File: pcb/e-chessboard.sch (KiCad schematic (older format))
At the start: 15 parts

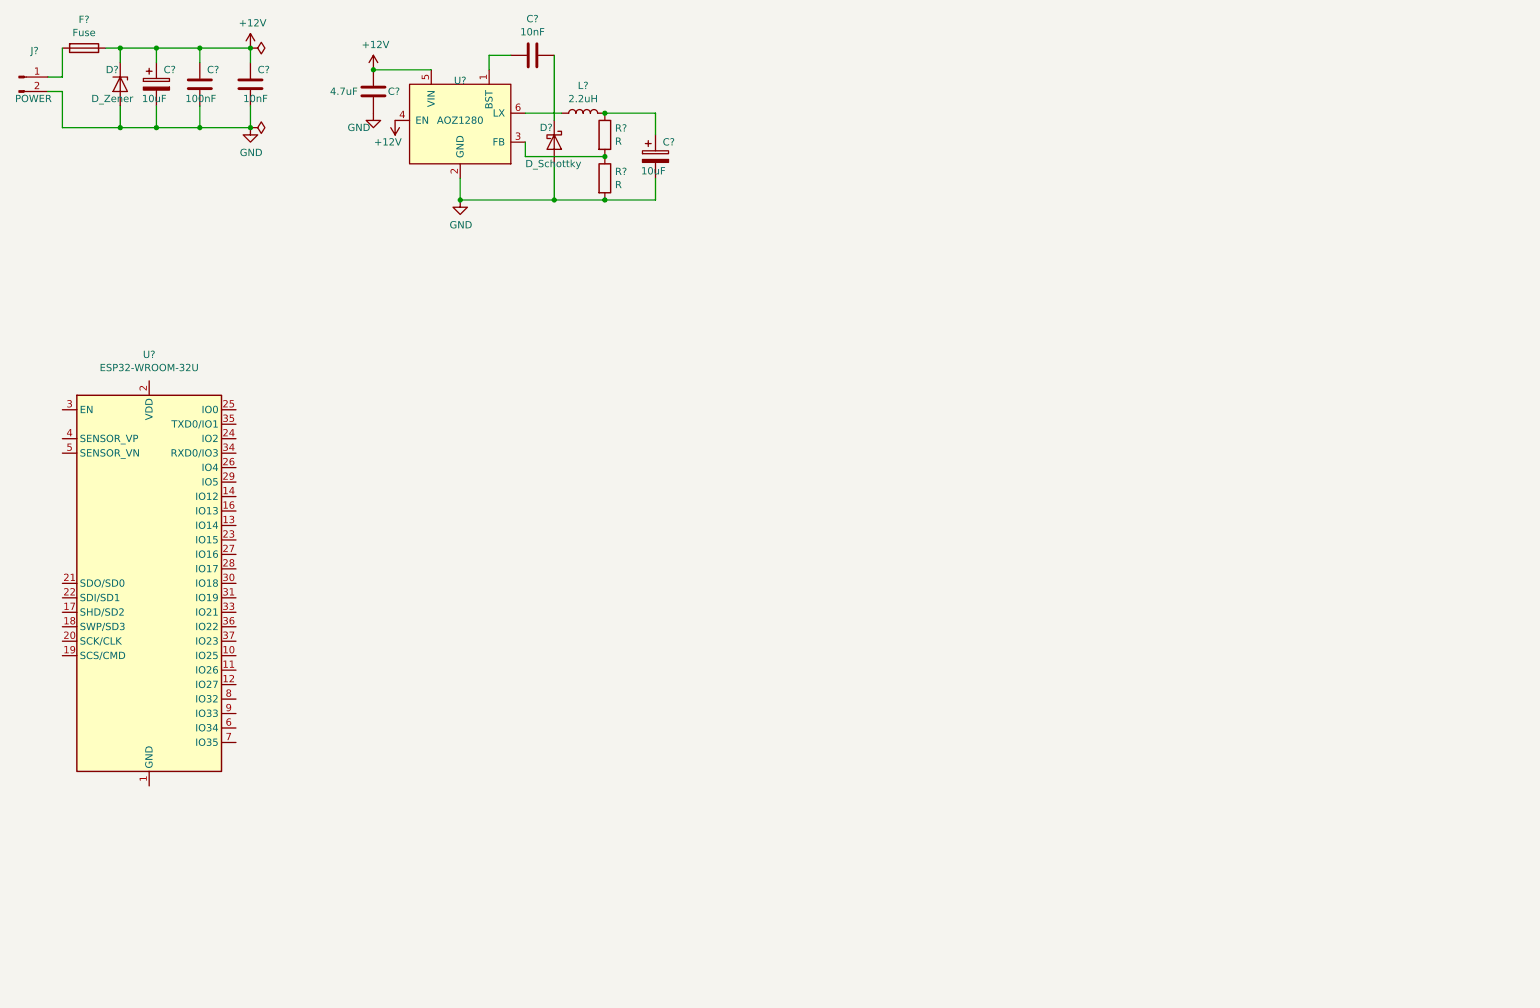
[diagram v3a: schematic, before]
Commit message: feat(kicad): adding magnet matrix and driver
Adding the 3x3 magnet matrix and the NCV7608 driver.
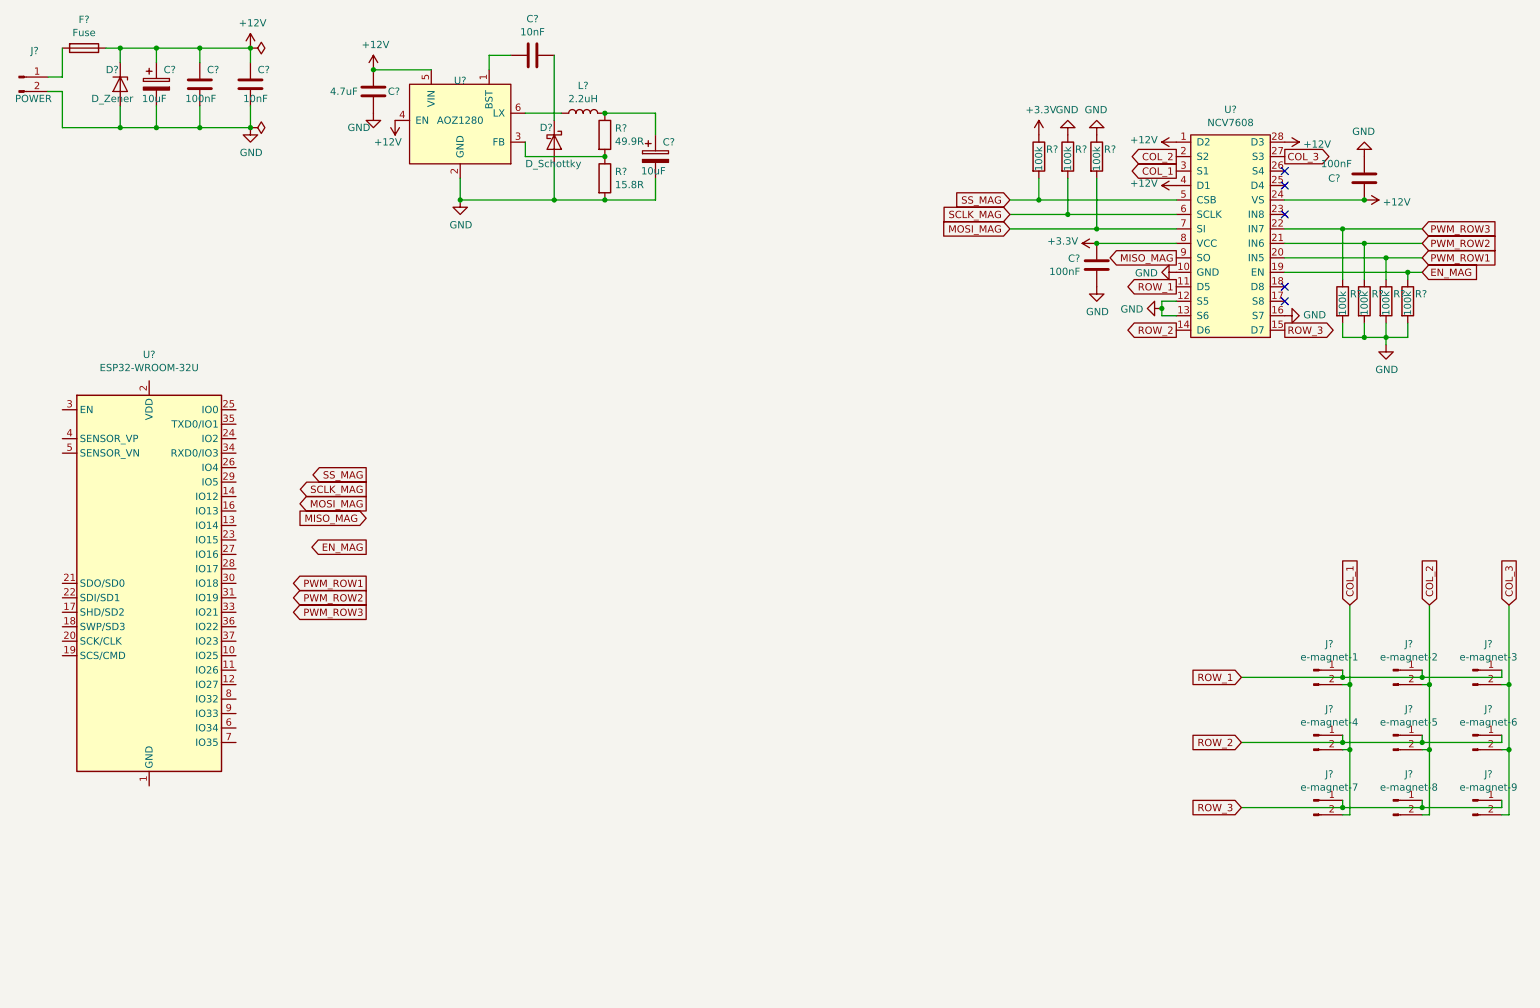
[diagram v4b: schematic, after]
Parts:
- added C? (x2): 100nF, symbol Device:C
- added J?: e-magnet-2, lib_fp:20_15_electromagnet, symbol Connector:Conn_01x02_Male
- added J?: e-magnet-5, lib_fp:20_15_electromagnet, symbol Connector:Conn_01x02_Male
- added J?: e-magnet-8, lib_fp:20_15_electromagnet, symbol Connector:Conn_01x02_Male
- added J?: e-magnet-4, lib_fp:20_15_electromagnet, symbol Connector:Conn_01x02_Male
- added J?: e-magnet-1, lib_fp:20_15_electromagnet, symbol Connector:Conn_01x02_Male
- added J?: e-magnet-3, lib_fp:20_15_electromagnet, symbol Connector:Conn_01x02_Male
- added J?: e-magnet-7, lib_fp:20_15_electromagnet, symbol Connector:Conn_01x02_Male
- added J?: e-magnet-6, lib_fp:20_15_electromagnet, symbol Connector:Conn_01x02_Male
- added J?: e-magnet-9, lib_fp:20_15_electromagnet, symbol Connector:Conn_01x02_Male
- added R? (x7): 100k, symbol Device:R
- added U?: NCV7608, Package_SO:SOIC-28W_7.5x17.9mm_P1.27mm, symbol lib:NCV7608
- R?: value R -> 49.9R
- R?: value R -> 15.8R
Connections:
- net +12V: now also C?.2, U?.1 (D2), U?.24 (VS), U?.28 (D3), U?.4 (D1)
- net GND: now also C?.1, C?.1, R?.1, R?.1, R?.2, R?.2, R?.2, R?.2, U?.10 (GND), U?.12 (S5), U?.13 (S6), U?.16 (S7)
- new net +3V3: C?.2, R?.1, U?.8 (VCC)
- new net COL_1: J?.2 (Pin_2), J?.2 (Pin_2), J?.2 (Pin_2), U?.3 (S1)
- new net COL_2: J?.2 (Pin_2), J?.2 (Pin_2), J?.2 (Pin_2), U?.2 (S2)
- new net COL_3: J?.2 (Pin_2), J?.2 (Pin_2), J?.2 (Pin_2), U?.27 (S3)
- new net EN_MAG: R?.1, U?.19 (EN)
- new net MISO_MAG: U?.9 (SO)
- new net MOSI_MAG: R?.2, U?.7 (SI)
- new net PWM_ROW1: R?.1, U?.20 (IN5)
- new net PWM_ROW2: R?.1, U?.21 (IN6)
- new net PWM_ROW3: R?.1, U?.22 (IN7)
- new net ROW_1: J?.1 (Pin_1), J?.1 (Pin_1), J?.1 (Pin_1), U?.11 (D5)
- new net ROW_2: J?.1 (Pin_1), J?.1 (Pin_1), J?.1 (Pin_1), U?.14 (D6)
- new net ROW_3: J?.1 (Pin_1), J?.1 (Pin_1), J?.1 (Pin_1), U?.15 (D7)
- new net SCLK_MAG: R?.2, U?.6 (SCLK)
- new net SS_MAG: R?.2, U?.5 (CSB)
- no-connect marks 0 -> 5

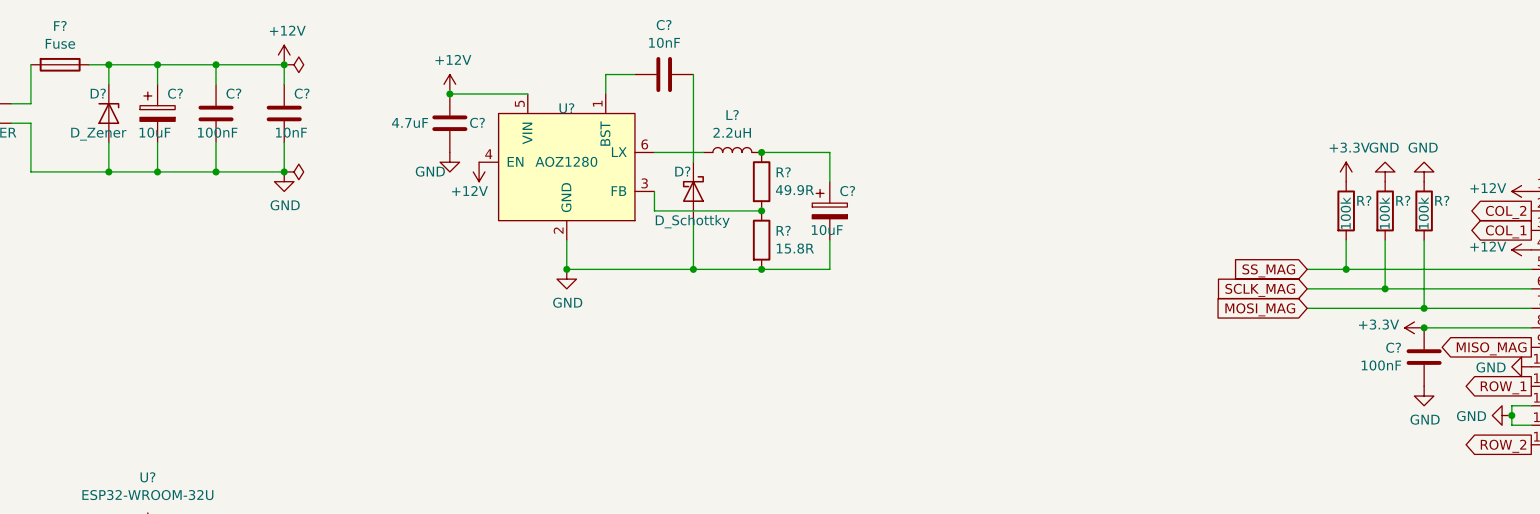
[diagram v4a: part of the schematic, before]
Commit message: fix(kicad): adding missing footprints
Adding C, R, L, D footprints
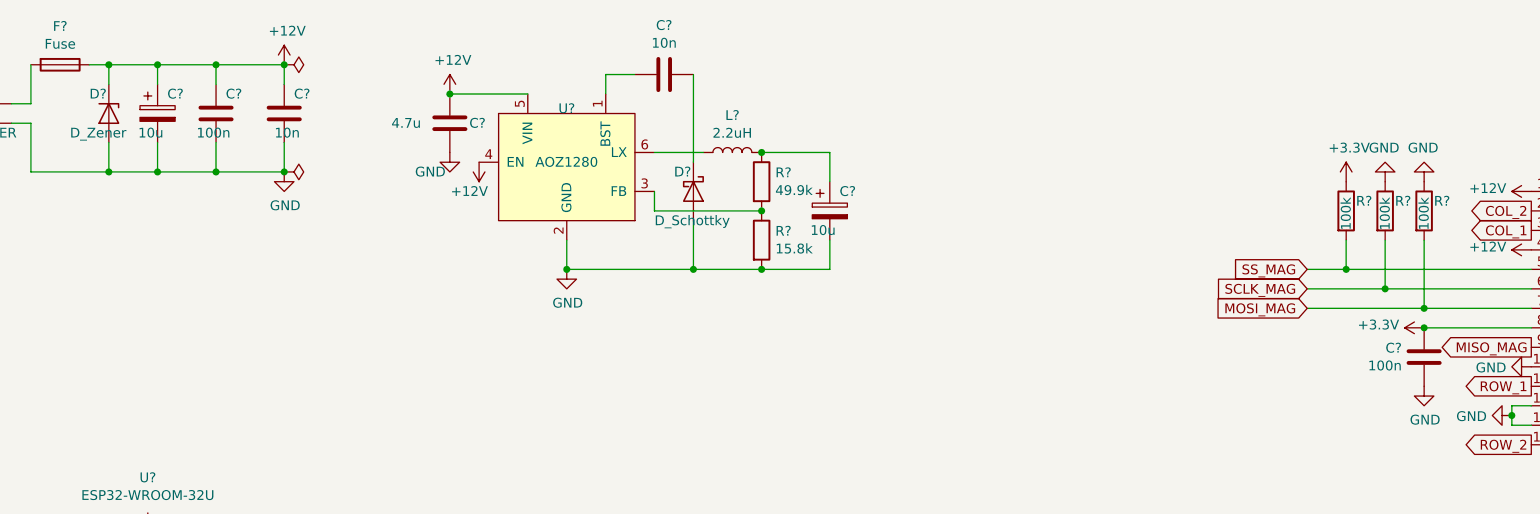
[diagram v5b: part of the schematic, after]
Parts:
- removed R? (x6): 100k, symbol Device:R
- added R? (x6): 100k, Resistor_SMD:R_0805_2012Metric, symbol Device:R
- C? (x2): value 100nF -> 100n; footprint (none) -> Capacitor_SMD:C_0805_2012Metric_Pad1.15x1.40mm_HandSolder
- C? (x2): value 10uF -> 10u; footprint (none) -> Capacitor_Tantalum_SMD:CP_EIA-3528-21_Kemet-B
- C? (x2): value 10nF -> 10n; footprint (none) -> Capacitor_SMD:C_0805_2012Metric_Pad1.15x1.40mm_HandSolder
- C?: value 4.7uF -> 4.7u; footprint (none) -> Capacitor_SMD:C_0805_2012Metric_Pad1.15x1.40mm_HandSolder
- C?: footprint (none) -> Capacitor_SMD:C_0805_2012Metric_Pad1.15x1.40mm_HandSolder
- D?: footprint (none) -> Diode_SMD:D_SOD-123
- D?: footprint (none) -> Diode_SMD:D_SMA
- L?: footprint (none) -> Inductor_SMD:L_Bourns-SRN4018
- R?: value 49.9R -> 49.9k; footprint (none) -> Resistor_SMD:R_0805_2012Metric
- R?: value 15.8R -> 15.8k; footprint (none) -> Resistor_SMD:R_0805_2012Metric
- R?: footprint (none) -> Resistor_SMD:R_0805_2012Metric
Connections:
- net +3V3: now also R?.1
- net EN_MAG: now also R?.1
- net GND: now also R?.1, R?.2, R?.2, R?.2, R?.2
- net PWM_ROW1: now also R?.1
- net PWM_ROW2: now also R?.1
- net PWM_ROW3: now also R?.1
- net SCLK_MAG: now also R?.2
- net SS_MAG: now also R?.2
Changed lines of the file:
@@
 P 1750 1150
 F 0 "C?" H 1800 1250 50  0000 L CNN
-F 1 "100nF" H 1650 1050 50  0000 L CNN
-F 2 "" H 1788 1000 50  0001 C CNN
+F 1 "100n" H 1650 1050 50  0000 L CNN
+F 2 "Capacitor_SMD:C_0805_2012Metric_Pad1.15x1.40mm_HandSolder" H 1788 1000 50  0001 C CNN
 F 3 "~" H 1750 1150 50  0001 C CNN
 	1    1750 1150
@@
 P 1450 1150
 F 0 "C?" H 1500 1250 50  0000 L CNN
-F 1 "10uF" H 1350 1050 50  0000 L CNN
-F 2 "" H 1488 1000 50  0001 C CNN
+F 1 "10u" H 1350 1050 50  0000 L CNN
+F 2 "Capacitor_Tantalum_SMD:CP_EIA-3528-21_Kemet-B" H 1488 1000 50  0001 C CNN
 F 3 "~" H 1450 1150 50  0001 C CNN
 	1    1450 1150
@@
 P 2100 1150
 F 0 "C?" H 2150 1250 50  0000 L CNN
-F 1 "10nF" H 2050 1050 50  0000 L CNN
-F 2 "" H 2138 1000 50  0001 C CNN
+F 1 "10n" H 2050 1050 50  0000 L CNN
+F 2 "Capacitor_SMD:C_0805_2012Metric_Pad1.15x1.40mm_HandSolder" H 2138 1000 50  0001 C CNN
 F 3 "~" H 2100 1150 50  0001 C CNN
 	1    2100 1150
@@
 P 2950 1200
 F 0 "C?" H 3050 1200 50  0000 L CNN
-F 1 "4.7uF" H 2650 1200 50  0000 L CNN
-F 2 "" H 2988 1050 50  0001 C CNN
+F 1 "4.7u" H 2650 1200 50  0000 L CNN
+F 2 "Capacitor_SMD:C_0805_2012Metric_Pad1.15x1.40mm_HandSolder" H 2988 1050 50  0001 C CNN
 F 3 "~" H 2950 1200 50  0001 C CNN
 	1    2950 1200
@@
 P 4050 950
 F 0 "C?" V 4302 950 50  0000 C CNN
-F 1 "10nF" V 4211 950 50  0000 C CNN
-F 2 "" H 4088 800 50  0001 C CNN
+F 1 "10n" V 4211 950 50  0000 C CNN
+F 2 "Capacitor_SMD:C_0805_2012Metric_Pad1.15x1.40mm_HandSolder" H 4088 800 50  0001 C CNN
 F 3 "~" H 4050 950 50  0001 C CNN
 	1    4050 950
@@
 F 0 "L?" V 4590 1350 50  0000 C CNN
 F 1 "2.2uH" V 4499 1350 50  0000 C CNN
-F 2 "" H 4400 1350 50  0001 C CNN
-F 3 "~" H 4400 1350 50  0001 C CNN
+F 2 "Inductor_SMD:L_Bourns-SRN4018" H 4400 1350 50  0001 C CNN
+F 3 "https://www.bourns.com/docs/Product-Datasheets/SRN4018.pdf" H 4400 1350 50  0001 C CNN
 	1    4400 1350
 	0    -1   -1   0
@@
 P 4900 1650
 F 0 "C?" H 4950 1750 50  0000 L CNN
-F 1 "10uF" H 4800 1550 50  0000 L CNN
-F 2 "" H 4938 1500 50  0001 C CNN
+F 1 "10u" H 4800 1550 50  0000 L CNN
+F 2 "Capacitor_Tantalum_SMD:CP_EIA-3528-21_Kemet-B" H 4938 1500 50  0001 C CNN
 F 3 "~" H 4900 1650 50  0001 C CNN
 	1    4900 1650
@@
 P 4550 1500
 F 0 "R?" H 4620 1546 50  0000 L CNN
-F 1 "49.9R" H 4620 1455 50  0000 L CNN
-F 2 "" V 4480 1500 50  0001 C CNN
+F 1 "49.9k" H 4620 1455 50  0000 L CNN
+F 2 "Resistor_SMD:R_0805_2012Metric" V 4480 1500 50  0001 C CNN
 F 3 "~" H 4550 1500 50  0001 C CNN
 	1    4550 1500
@@
 P 4550 1800
 F 0 "R?" H 4620 1846 50  0000 L CNN
-F 1 "15.8R" H 4620 1755 50  0000 L CNN
-F 2 "" V 4480 1800 50  0001 C CNN
+F 1 "15.8k" H 4620 1755 50  0000 L CNN
+F 2 "Resistor_SMD:R_0805_2012Metric" V 4480 1800 50  0001 C CNN
 F 3 "~" H 4550 1800 50  0001 C CNN
 	1    4550 1800
@@
 F 0 "D?" V 4100 1450 50  0000 L CNN
 F 1 "D_Schottky" V 4350 1350 50  0000 L CNN
-F 2 "" H 4200 1550 50  0001 C CNN
+F 2 "Diode_SMD:D_SOD-123" H 4200 1550 50  0001 C CNN
 F 3 "~" H 4200 1550 50  0001 C CNN
 	1    4200 1550
@@
 F 0 "D?" V 1100 1050 50  0000 L CNN
 F 1 "D_Zener" V 1300 950 50  0000 L CNN
-F 2 "" H 1200 1150 50  0001 C CNN
-F 3 "~" H 1200 1150 50  0001 C CNN
+F 2 "Diode_SMD:D_SMA" H 1200 1150 50  0001 C CNN
+F 3 "https://www.diodes.com/assets/Datasheets/ds18015.pdf" H 1200 1150 50  0001 C CNN
 	1    1200 1150
 	0    1    1    0
@@
 F 0 "C?" H 10050 1800 50  0000 R CNN
 F 1 "100nF" H 10100 1900 50  0000 R CNN
-F 2 "" H 9838 1650 50  0001 C CNN
+F 2 "Capacitor_SMD:C_0805_2012Metric_Pad1.15x1.40mm_HandSolder" H 9838 1650 50  0001 C CNN
 F 3 "~" H 9800 1800 50  0001 C CNN
 	1    9800 1800
@@
 F 0 "R?" H 8000 1700 50  0000 L CNN
 F 1 "100k" V 7950 1550 50  0000 L CNN
-F 2 "" V 7880 1650 50  0001 C CNN
+F 2 "Resistor_SMD:R_0805_2012Metric" V 7880 1650 50  0001 C CNN
 F 3 "~" H 7950 1650 50  0001 C CNN
 	1    7950 1650
-	1    0    0    -1
-$EndComp
-$Comp
-L Device:R R?
-U 1 1 5E6E973A
-P 7750 1650
-F 0 "R?" H 7800 1700 50  0000 L CNN
-F 1 "100k" V 7750 1550 50  0000 L CNN
-F 2 "" V 7680 1650 50  0001 C CNN
-F 3 "~" H 7750 1650 50  0001 C CNN
-	1    7750 1650
-	1    0    0    -1
-$EndComp
-$Comp
-L Device:R R?
-U 1 1 5E6E9902
-P 7550 1650
-F 0 "R?" H 7600 1700 50  0000 L CNN
-F 1 "100k" V 7550 1550 50  0000 L CNN
-F 2 "" V 7480 1650 50  0001 C CNN
-F 3 "~" H 7550 1650 50  0001 C CNN
-	1    7550 1650
 	1    0    0    -1
 $EndComp
@@
 P 7950 2400
 F 0 "C?" H 7836 2354 50  0000 R CNN
-F 1 "100nF" H 7836 2445 50  0000 R CNN
-F 2 "" H 7988 2250 50  0001 C CNN
+F 1 "100n" H 7836 2445 50  0000 R CNN
+F 2 "Capacitor_SMD:C_0805_2012Metric_Pad1.15x1.40mm_HandSolder" H 7988 2250 50  0001 C CNN
 F 3 "~" H 7950 2400 50  0001 C CNN
 	1    7950 2400
@@
 $EndComp
 $Comp
-L Device:R R?
-U 1 1 5E73BE4D
-P 9950 2650
-F 0 "R?" H 10000 2700 50  0000 L CNN
-F 1 "100k" V 9950 2550 50  0000 L CNN
-F 2 "" V 9880 2650 50  0001 C CNN
-F 3 "~" H 9950 2650 50  0001 C CNN
-	1    9950 2650
-	1    0    0    -1
-$EndComp
-$Comp
-L Device:R R?
-U 1 1 5E73C4B3
-P 9800 2650
-F 0 "R?" H 9850 2700 50  0000 L CNN
-F 1 "100k" V 9800 2550 50  0000 L CNN
-F 2 "" V 9730 2650 50  0001 C CNN
-F 3 "~" H 9800 2650 50  0001 C CNN
-	1    9800 2650
-	1    0    0    -1
-$EndComp
-$Comp
-L Device:R R?
-U 1 1 5E73C813
-P 9650 2650
-F 0 "R?" H 9700 2700 50  0000 L CNN
-F 1 "100k" V 9650 2550 50  0000 L CNN
-F 2 "" V 9580 2650 50  0001 C CNN
-F 3 "~" H 9650 2650 50  0001 C CNN
-	1    9650 2650
-	1    0    0    -1
-$EndComp
-$Comp
 L power:GND #PWR?
 U 1 1 5E750D06
@@
 Wire Wire Line
 	9950 2350 9250 2350
+Wire Wire Line
+	9250 1950 9800 1950
+Connection ~ 9800 1950
+Wire Wire Line
+	9950 2350 10200 2350
+Wire Wire Line
+	9800 2250 10200 2250
+Wire Wire Line
+	9650 2150 10200 2150
+Wire Wire Line
+	10200 2450 10100 2450
+Wire Wire Line
+	10100 2500 10100 2450
+Connection ~ 10100 2450
+Wire Wire Line
+	10100 2450 9250 2450
+Wire Wire Line
+	10100 2800 10100 2900
+Wire Wire Line
+	10100 2900 9950 2900
 $Comp
 L Device:R R?
-U 1 1 5E77C75A
+U 1 1 5E850D8B
+P 7750 1650
+F 0 "R?" H 7800 1700 50  0000 L CNN
+F 1 "100k" V 7750 1550 50  0000 L CNN
+F 2 "Resistor_SMD:R_0805_2012Metric" V 7680 1650 50  0001 C CNN
+F 3 "~" H 7750 1650 50  0001 C CNN
+	1    7750 1650
+	1    0    0    -1
+$EndComp
+$Comp
+L Device:R R?
+U 1 1 5E850F87
+P 7550 1650
+F 0 "R?" H 7600 1700 50  0000 L CNN
+F 1 "100k" V 7550 1550 50  0000 L CNN
+F 2 "Resistor_SMD:R_0805_2012Metric" V 7480 1650 50  0001 C CNN
+F 3 "~" H 7550 1650 50  0001 C CNN
+	1    7550 1650
+	1    0    0    -1
+$EndComp
+$Comp
+L Device:R R?
+U 1 1 5E8512EB
+P 9650 2650
+F 0 "R?" H 9700 2700 50  0000 L CNN
+F 1 "100k" V 9650 2550 50  0000 L CNN
+F 2 "Resistor_SMD:R_0805_2012Metric" V 9580 2650 50  0001 C CNN
+F 3 "~" H 9650 2650 50  0001 C CNN
+	1    9650 2650
+	1    0    0    -1
+$EndComp
+$Comp
+L Device:R R?
+U 1 1 5E858158
+P 9800 2650
+F 0 "R?" H 9850 2700 50  0000 L CNN
+F 1 "100k" V 9800 2550 50  0000 L CNN
+F 2 "Resistor_SMD:R_0805_2012Metric" V 9730 2650 50  0001 C CNN
+F 3 "~" H 9800 2650 50  0001 C CNN
+	1    9800 2650
+	1    0    0    -1
+$EndComp
+$Comp
+L Device:R R?
+U 1 1 5E85848F
+P 9950 2650
+F 0 "R?" H 10000 2700 50  0000 L CNN
+F 1 "100k" V 9950 2550 50  0000 L CNN
+F 2 "Resistor_SMD:R_0805_2012Metric" V 9880 2650 50  0001 C CNN
+F 3 "~" H 9950 2650 50  0001 C CNN
+	1    9950 2650
+	1    0    0    -1
+$EndComp
+$Comp
+L Device:R R?
+U 1 1 5E85871C
 P 10100 2650
 F 0 "R?" H 10150 2700 50  0000 L CNN
 F 1 "100k" V 10100 2550 50  0000 L CNN
-F 2 "" V 10030 2650 50  0001 C CNN
+F 2 "Resistor_SMD:R_0805_2012Metric" V 10030 2650 50  0001 C CNN
 F 3 "~" H 10100 2650 50  0001 C CNN
 	1    10100 2650
 	1    0    0    -1
 $EndComp
-Wire Wire Line
-	9250 1950 9800 1950
-Connection ~ 9800 1950
-Wire Wire Line
-	9950 2350 10200 2350
-Wire Wire Line
-	9800 2250 10200 2250
-Wire Wire Line
-	9650 2150 10200 2150
-Wire Wire Line
-	10200 2450 10100 2450
-Wire Wire Line
-	10100 2500 10100 2450
-Connection ~ 10100 2450
-Wire Wire Line
-	10100 2450 9250 2450
-Wire Wire Line
-	10100 2800 10100 2900
-Wire Wire Line
-	10100 2900 9950 2900
 $EndSCHEMATC

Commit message: feat(kicad): adding uart programmer
Adding the UART programmer to the eps32.
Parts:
- added C? (x2): 100nF, Capacitor_SMD:C_0805_2012Metric_Pad1.15x1.40mm_HandSolder, symbol Device:C
- added J?: UART, Connector_PinHeader_2.54mm:PinHeader_2x03_P2.54mm_Vertical, symbol Connector:Conn_01x06_Male
- added Q? (x3): BC847, Package_TO_SOT_SMD:SOT-23, symbol Transistor_BJT:BC847
- added R? (x5): 10k, Resistor_SMD:R_0805_2012Metric, symbol Device:R
- added SW?: SW_Push, Button_Switch_SMD:SW_SPST_EVQPE1, symbol Switch:SW_Push
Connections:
- net +3V3: now also J?.1 (Pin_1), R?.2, R?.2
- net GND: now also C?.1, C?.2, J?.2 (Pin_2), SW?.2
- net IO0: now reaches U?.25 (IO0)
- net IO0: now also C?.2, Q?.3 (C), R?.1, SW?.1
- net EN: now reaches U?.3 (EN)
- net EN: now also C?.1, Q?.3 (C), R?.1
- new net: Q?.1 (B), Q?.2 (E), R?.1 (x2)
- new net DTR: J?.6 (Pin_6), R?.2
- new net RTS: J?.5 (Pin_5), R?.2
- new net UART_RX: J?.3 (Pin_3)
- new net UART_TX: J?.4 (Pin_4)
